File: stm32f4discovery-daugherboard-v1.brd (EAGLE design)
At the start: 100 x 70 mm, 44 parts

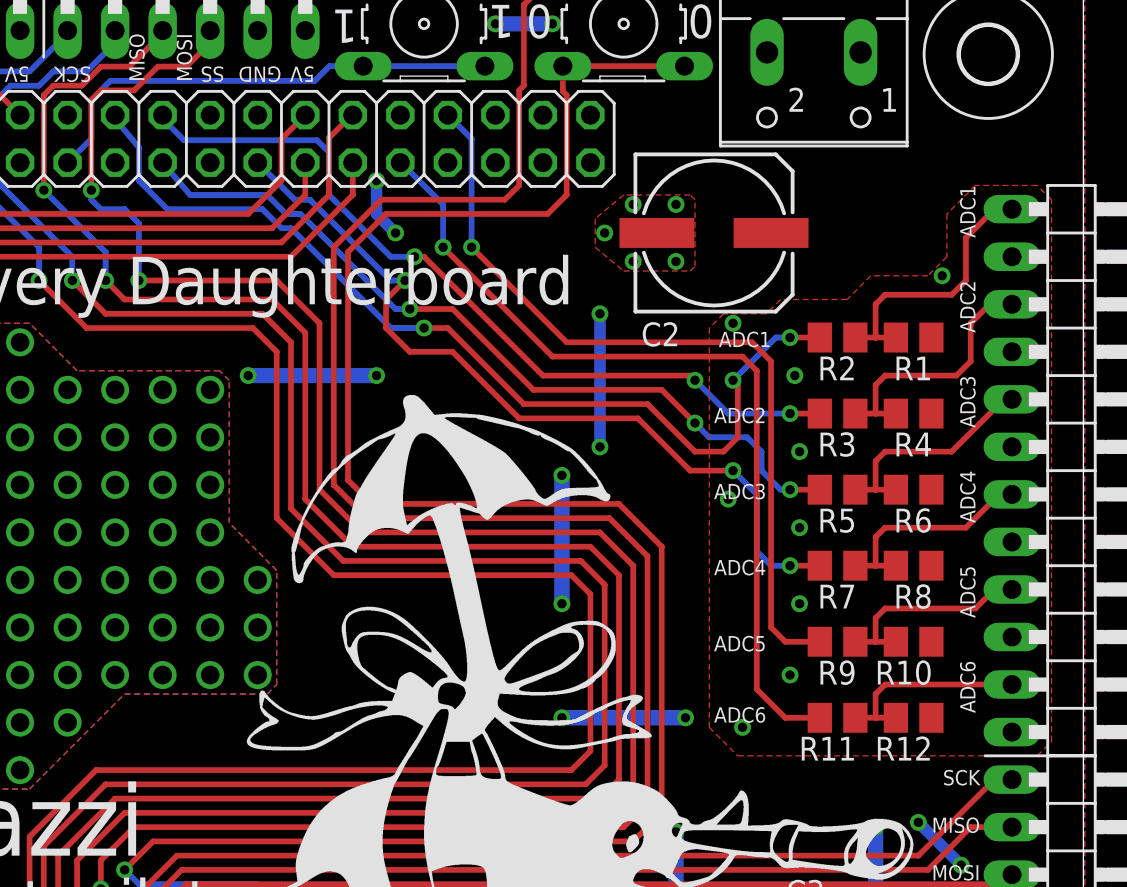
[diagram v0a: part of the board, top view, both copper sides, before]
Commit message: corrected adc voltage divider
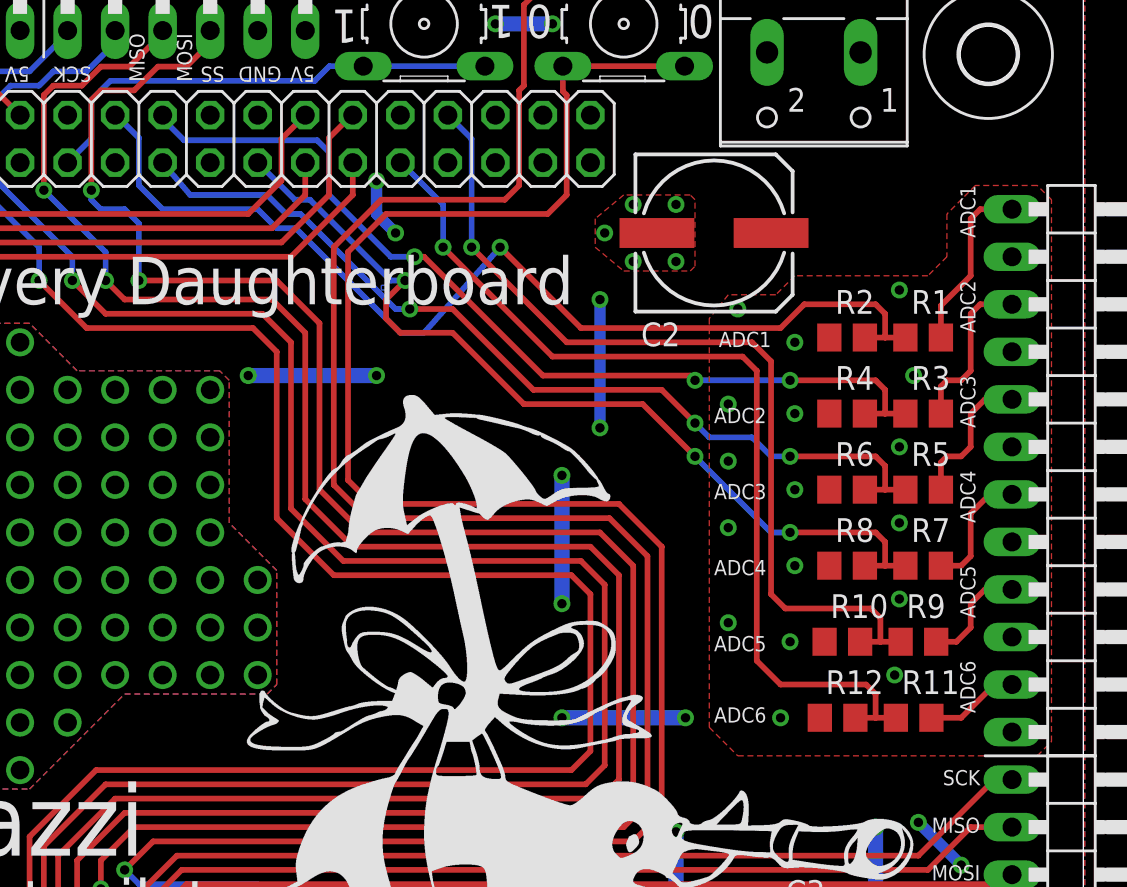
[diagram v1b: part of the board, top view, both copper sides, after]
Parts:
- R1: value 2k2 -> 10k; device resistor:M0805 -> rcl:R0805
- R10, R11, R12, R3, R4, R5, R6, R7, R8, R9: device resistor:M0805 -> rcl:R0805
- R2: value 10k -> 2k2; device resistor:M0805 -> rcl:R0805
- moved R3 4.57 mm to (91.4, 45.7), turned to 0 degrees
- moved R5 4.57 mm to (91.4, 41.7), turned to 0 degrees
- moved R7 4.57 mm to (91.4, 37.6), turned to 0 degrees
- moved R9 4.32 mm to (91.2, 33.5), turned to 0 degrees
- moved R11 4.06 mm to (90.9, 29.5), turned to 0 degrees
- moved R12 4.06 mm to (86.9, 29.5), turned to 0 degrees
- moved R10 3.81 mm to (87.1, 33.5), turned to 0 degrees
- moved R4 3.56 mm to (87.4, 45.7), turned to 0 degrees
- moved R6 3.56 mm to (87.4, 41.7), turned to 0 degrees
- moved R8 3.56 mm to (87.4, 37.6), turned to 0 degrees
- moved R2 0.51 mm to (87.4, 49.8), turned to 0 degrees
- moved R1 0.51 mm to (91.4, 49.8), turned to 0 degrees
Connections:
- net ADC1: no longer R2.1
- net ADC2: now also R3.2; no longer R3.1, R4.2
- net ADC3: now also R5.2; no longer R5.1, R6.2
- net ADC4: now also R7.2; no longer R7.1, R8.2
- net ADC5: now also R9.2; no longer R10.2, R9.1
- net ADC6: now also R11.2; no longer R11.1, R12.2
- net GND: now also R2.1; no longer R1.1
- net PA4: now also R7.1, R8.2; no longer R7.2
- net PB1: now also R1.1
- net PC1: now also R10.2, R9.1; no longer R9.2
- net PC2: now also R11.1, R12.2; no longer R11.2
- net PC4: now also R5.1, R6.2; no longer R5.2
- net PC5: now also R3.1, R4.2; no longer R3.2
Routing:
- net PC5: track 43.2 -> 49.6 mm
- net ADC6: track 10.9 -> 5.04 mm
- net PC4: track 43.0 -> 48.8 mm
- net ADC5: track 11.4 -> 5.96 mm
- net ADC1: track 14.7 -> 9.43 mm
- net ADC4: track 11.9 -> 6.72 mm
- net PC1: track 43.3 -> 48.4 mm
- net ADC2: track 14.0 -> 8.86 mm
- net PC2: track 46.0 -> 51.0 mm
- net ADC3: track 12.3 -> 7.69 mm
- net PB1: track 51.0 -> 55.5 mm, vias 3 -> 1
- net PA4: track 43.7 -> 48.0 mm
- added copper zone on layer 1, net ADC3
- added copper zone on layer 16, net ADC5
- added copper zone on layer 16, net ADC6
- added copper zone on layer 16, net N$1
- removed copper zone on layer 1, net N$12
- removed copper zone on layer 1, net N$15
- removed copper zone on layer 16, net N$17
- removed copper zone on layer 16, net N$18

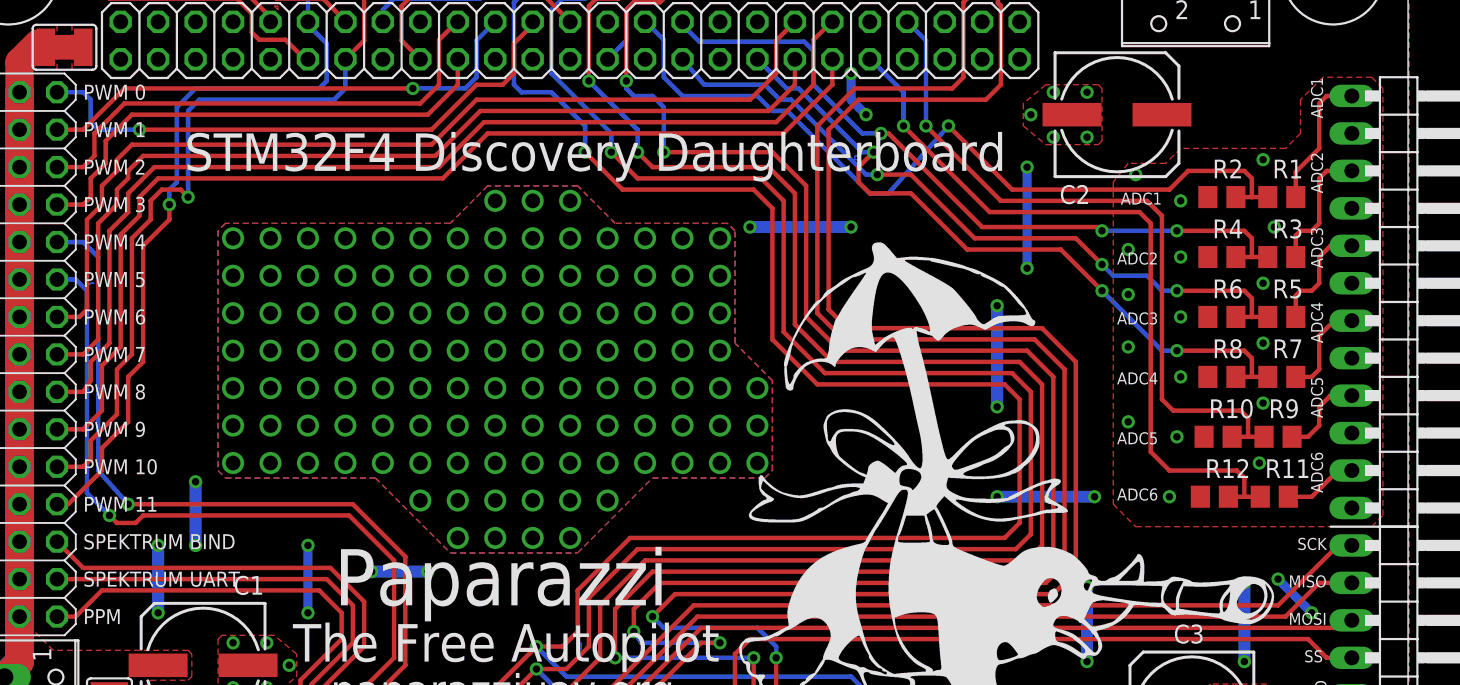
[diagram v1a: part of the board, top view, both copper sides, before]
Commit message: added suppressor diode on all adc
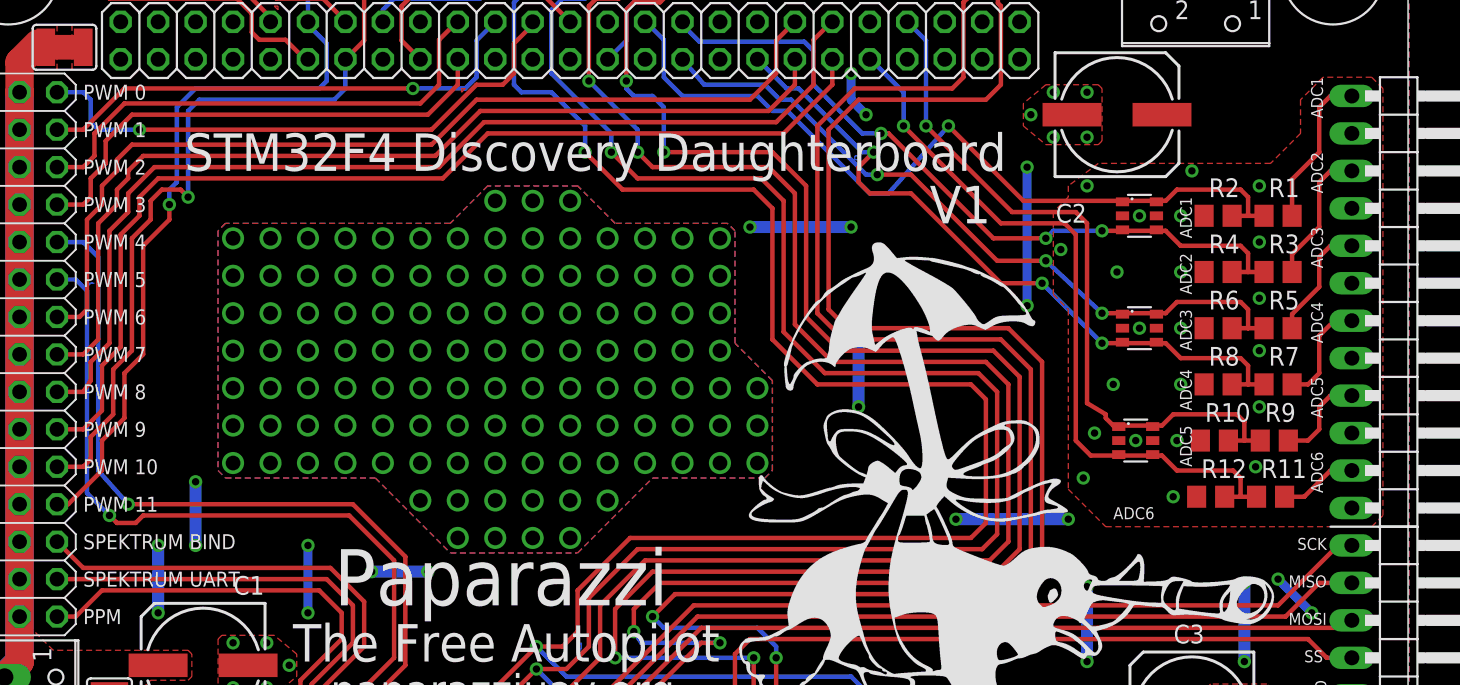
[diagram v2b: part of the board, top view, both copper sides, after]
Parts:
- added U$4, U$5, U$6: ESDA5V3SC6, suppressor diode:SOT23-6
- moved R2 1.30 mm to (87.1, 48.5)
- moved R1 1.30 mm to (91.2, 48.5)
- moved R4 1.05 mm to (87.1, 44.7)
- moved R3 1.05 mm to (91.2, 44.7)
- moved R6 0.80 mm to (87.1, 40.9)
- moved R5 0.80 mm to (91.2, 40.9)
- moved R8 0.57 mm to (87.1, 37.1)
- moved R7 0.57 mm to (91.2, 37.1)
- moved R10 0.36 mm to (86.9, 33.3)
- moved R9 0.36 mm to (90.9, 33.3)
- moved R11 0.25 mm to (90.7, 29.5)
- moved R12 0.25 mm to (86.6, 29.5)
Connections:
- net GND: now also U$4.2, U$4.5, U$5.2, U$5.5, U$6.2, U$6.5
- net PA4: now also U$5.3, U$5.4
- net PB1: now also U$4.1, U$4.6
- net PC1: now also U$6.1, U$6.6
- net PC2: now also U$6.3, U$6.4
- net PC4: now also U$5.1, U$5.6
- net PC5: now also U$4.3, U$4.4
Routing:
- net PE3: track 125.1 -> 120.2 mm
- net BOOT0: track 124.2 -> 119.4 mm
- net PC12: track 135.1 -> 130.4 mm
- net PC10: track 164.0 -> 159.5 mm
- net PC11: track 163.1 -> 158.5 mm
- net 3V: track 131.5 -> 126.9 mm
- net VIN: track 70.9 -> 74.4 mm
- net ADC1: track 9.43 -> 10.7 mm
- net PC2: track 51.0 -> 49.9 mm
- net PC4: track 48.8 -> 49.5 mm
- net ADC4: track 6.72 -> 7.33 mm
- net PC5: track 49.6 -> 50.2 mm
- net ADC2: track 8.86 -> 9.39 mm
- net ADC5: track 5.96 -> 6.46 mm
- added copper zone on layer 1, net N$3
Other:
- board text added: "V1"

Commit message: input protection
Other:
- board text added: "this version it not up to date, look at the tht version !!!"
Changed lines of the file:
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@@
 <text x="67.564" y="48.006" size="2.54" layer="25">V1</text>
 <text x="71.628" y="48.006" size="2.54" layer="26" rot="MR0">V1</text>
+<text x="-16.51" y="84.074" size="6.4516" layer="25">this version it not up to date, look at the tht version !!!</text>
 </plain>
 <attributes>
